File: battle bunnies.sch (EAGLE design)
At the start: 59 parts, among them IC1 CP2104, Q1 mmbt2222, Q2 mmbt2222, SW2 KMR2, U1 PCA9685, U2 SPX3819, U3 MCP73831T-2ACI/OT, X2 ESP-12, X4 20329

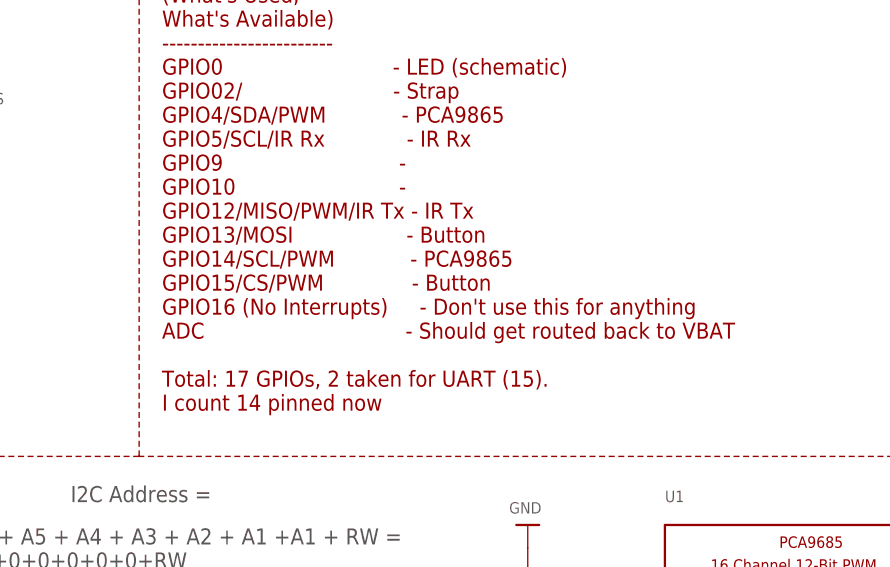
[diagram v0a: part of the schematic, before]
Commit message: USB: Swapping the USB part out - twas unobtanium
The 4UCONN connector that Adafruit used is basically made of unobtanium
and more or less doesn't exist.  The part that was trying to be used
the rear prongs did not match up by any stretch of the imagination.

A mess of e-mails an annoyance ensued.

I'm swapping out the part on everything I can now, this seems to be
more common, and there's parts that are similar enough to it that
replacing it won't be a big deal.  New part is the
Amphenol FCI 10118193-0001LF
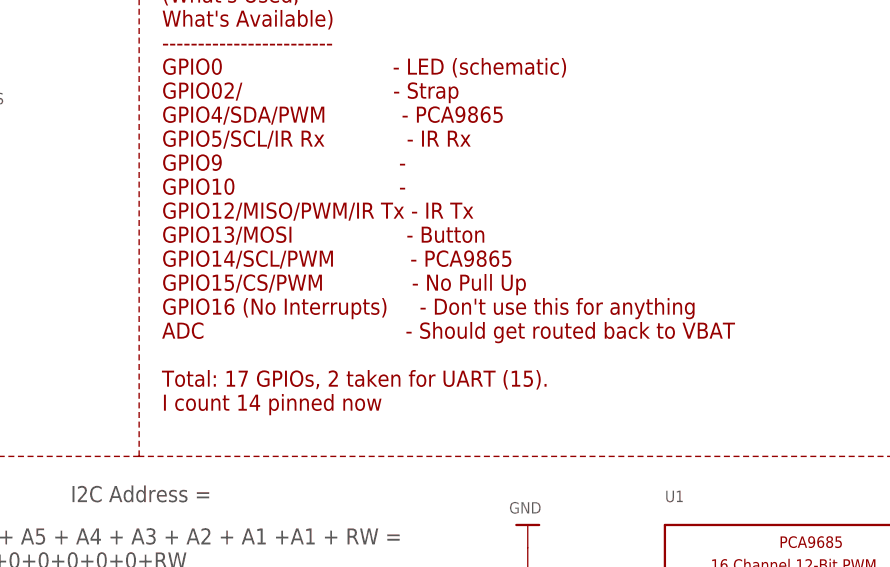
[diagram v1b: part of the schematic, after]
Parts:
- X4: device microbuilder:USB_MICRO_20329_V2 -> microbuilder:MICRO-USB-SMD-B-(10118193-0001LF)-ADASYM
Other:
- note added: "GPIO Table (What's Used, What's Available) ------------------------ GPIO0 - LED (schematic) GPIO02/ - Strap GPIO4/SDA/PWM - PCA9865 GPIO5/SCL/IR Rx - IR Rx GPIO9 - GPIO10 - GPIO12/MISO/PWM/IR Tx - IR Tx GPIO13/MOSI - Button GPIO14/SCL/PWM - PCA9865 GPIO15/CS/PWM - No Pull Up GPIO16 (No Interrupts) - Don't use this for anything ADC - Should get routed back to VBAT Total: 17 GPIOs, 2 taken for UART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"
- note removed: "GPIO Table (What's Used, What's Available) ------------------------ GPIO0 - LED (schematic) GPIO02/ - Strap GPIO4/SDA/PWM - PCA9865 GPIO5/SCL/IR Rx - IR Rx GPIO9 - GPIO10 - GPIO12/MISO/PWM/IR Tx - IR Tx GPIO13/MOSI - Button GPIO14/SCL/PWM - PCA9865 GPIO15/CS/PWM - Button GPIO16 (No Interrupts) - Don't use this for anything ADC - Should get routed back to VBAT Total: 17 GPIOs, 2 taken for UART (15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"
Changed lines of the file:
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@@
 <layer number="59" name="tCarbon" color="7" fill="1" visible="no" active="no"/>
 <layer number="60" name="bCarbon" color="7" fill="1" visible="no" active="no"/>
+<layer number="88" name="SimResults" color="7" fill="1" visible="yes" active="yes"/>
+<layer number="89" name="SimProbes" color="7" fill="1" visible="yes" active="yes"/>
 <layer number="90" name="Modules" color="5" fill="1" visible="yes" active="yes"/>
 <layer number="91" name="Nets" color="2" fill="1" visible="yes" active="yes"/>
@@
 <layer number="115" name="ReferenceISLANDS" color="7" fill="1" visible="yes" active="yes"/>
 <layer number="116" name="Patch_BOT" color="9" fill="4" visible="yes" active="yes"/>
+<layer number="117" name="BACKMAAT1" color="7" fill="1" visible="no" active="no"/>
 <layer number="118" name="Rect_Pads" color="7" fill="1" visible="yes" active="yes"/>
+<layer number="119" name="KAP_TEKEN" color="7" fill="1" visible="no" active="no"/>
+<layer number="120" name="KAP_MAAT1" color="7" fill="1" visible="no" active="no"/>
 <layer number="121" name="_tsilk" color="7" fill="1" visible="yes" active="yes"/>
 <layer number="122" name="_bsilk" color="7" fill="1" visible="yes" active="yes"/>
@@
 <layer number="128" name="_bValues" color="7" fill="1" visible="yes" active="yes"/>
 <layer number="129" name="Mask" color="7" fill="1" visible="yes" active="yes"/>
+<layer number="130" name="SMDSTROOK" color="7" fill="1" visible="no" active="no"/>
 <layer number="131" name="tAdjust" color="7" fill="1" visible="yes" active="yes"/>
 <layer number="132" name="bAdjust" color="7" fill="1" visible="yes" active="yes"/>
+<layer number="133" name="bottom_silk" color="7" fill="1" visible="no" active="no"/>
 <layer number="144" name="Drill_legend" color="7" fill="1" visible="yes" active="yes"/>
+<layer number="145" name="DrillLegend_01-16" color="7" fill="1" visible="yes" active="yes"/>
 <layer number="150" name="Notes" color="7" fill="1" visible="yes" active="yes"/>
 <layer number="151" name="HeatSink" color="7" fill="1" visible="yes" active="yes"/>
@@
 <part name="U$10" library="microbuilder" deviceset="3.3V" device=""/>
 <part name="IC1" library="microbuilder" deviceset="CP2104" device="" value="CP2104"/>
-<part name="X4" library="microbuilder" deviceset="USB" device="_MICRO_20329_V2" value="20329"/>
+<part name="X4" library="microbuilder" deviceset="MICRO-USB-SMD-B-(10118193-0001LF)-ADASYM" device="" value="20329"/>
 <part name="U$11" library="microbuilder" deviceset="GND" device=""/>
 <part name="U$12" library="microbuilder" deviceset="GND" device=""/>
@@
 GPIO13/MOSI                  - Button
 GPIO14/SCL/PWM            - PCA9865
-GPIO15/CS/PWM              - Button
+GPIO15/CS/PWM              - No Pull Up
 GPIO16 (No Interrupts)     - Don't use this for anything
 ADC                                - Should get routed back to VBAT
